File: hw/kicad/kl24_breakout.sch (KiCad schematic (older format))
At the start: 8 parts

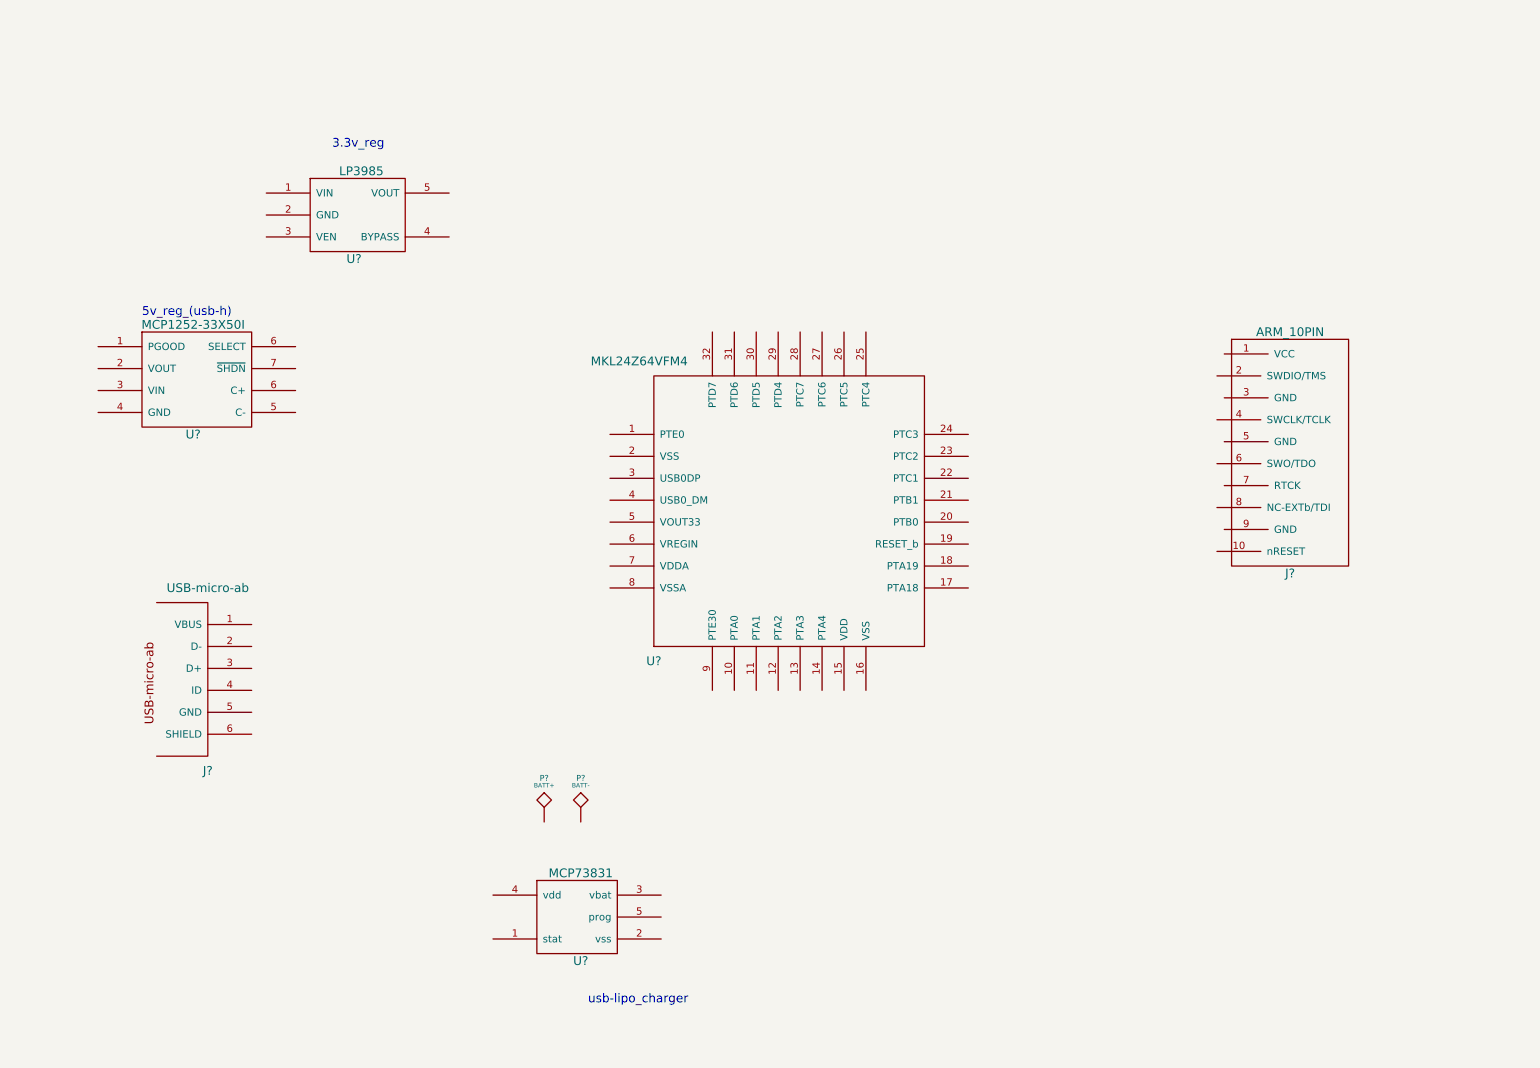
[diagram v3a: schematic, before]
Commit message: - add 0.9v lv battery powered supply (probably nopop)
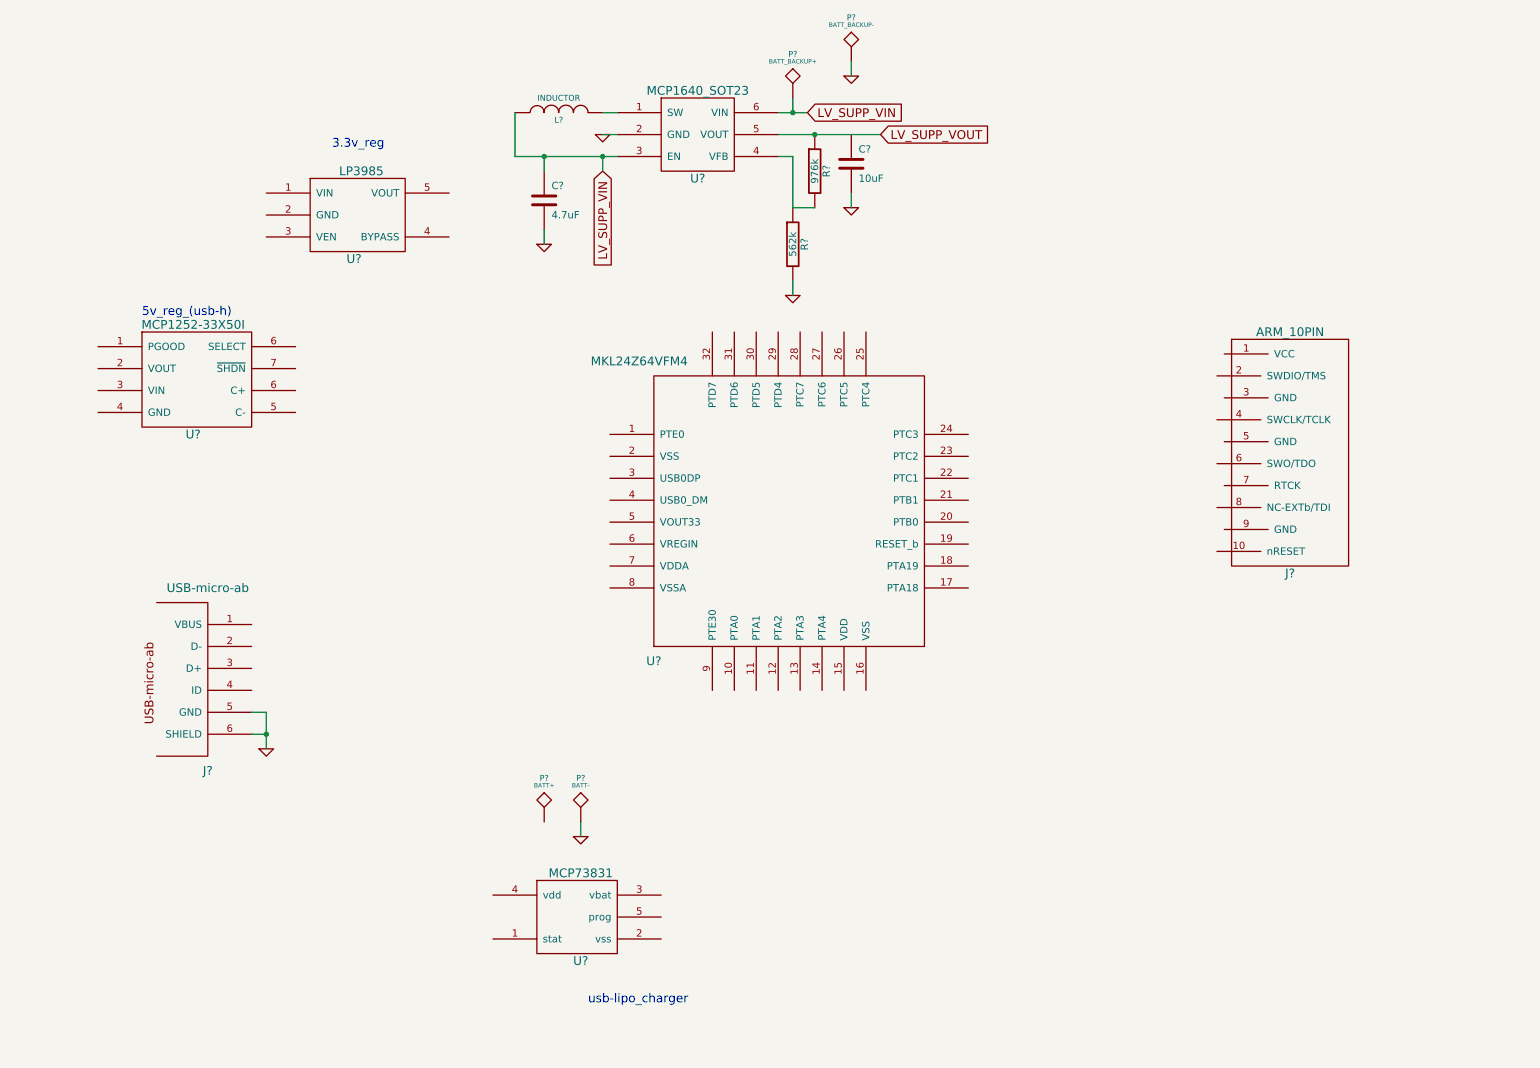
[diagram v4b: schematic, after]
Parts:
- added C?: 4.7uF, symbol C
- added C?: 10uF, symbol C
- added L?: INDUCTOR, symbol INDUCTOR
- added P?: BATT_BACKUP+, symbol TST
- added P?: BATT_BACKUP-, symbol TST
- added R?: 976k, symbol R
- added R?: 562k, symbol R
- added U?: MCP1640_SOT23, symbol MCP1640_SOT23
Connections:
- net GND: now reaches J?.5 (GND)
- net GND: now also J?.6 (SHIELD), P?.1, C?.2, C?.2, P?.1, R?.2, U?.2 (GND)
- new net: L?.2, U?.1 (SW)
- new net: R?.1, R?.2, U?.4 (VFB)
- new net LV_SUPP_VIN: C?.1, L?.1, P?.1, U?.3 (EN), U?.6 (VIN)
- new net LV_SUPP_VOUT: R?.1, U?.5 (VOUT)
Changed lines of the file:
@@
-EESchema Schematic File Version 2  date 3/5/2013 1:18:51 PM
+EESchema Schematic File Version 2  date 3/9/2013 12:18:49 PM
 LIBS:power
 LIBS:device
@@
 Sheet 1 1
 Title ""
-Date "5 mar 2013"
+Date "9 mar 2013"
 Rev ""
 Comp ""
@@
 Comment4 ""
 $EndDescr
+Connection ~ 4250 1400
+Wire Wire Line
+	4750 1400 4050 1400
+Wire Wire Line
+	4050 1400 4050 1100
+Wire Wire Line
+	4250 1400 4250 1500
+Wire Wire Line
+	6350 1650 6350 1750
+Wire Wire Line
+	5950 2250 5950 2350
+Wire Wire Line
+	6100 1750 5950 1750
+Wire Wire Line
+	4650 1250 4750 1250
+Wire Wire Line
+	4650 1400 4650 1500
+Wire Wire Line
+	5950 1100 5950 1000
+Wire Wire Line
+	2350 5350 2250 5350
+Wire Wire Line
+	6350 750  6350 850
+Wire Wire Line
+	4500 6050 4500 5950
+Wire Wire Line
+	2250 5200 2350 5200
+Wire Wire Line
+	2350 5200 2350 5450
+Connection ~ 2350 5350
+Wire Wire Line
+	6050 1100 5850 1100
+Connection ~ 5950 1100
+Connection ~ 4650 1400
+Wire Wire Line
+	5950 1750 5950 1400
+Wire Wire Line
+	5950 1400 5850 1400
+Connection ~ 6100 1250
+Wire Wire Line
+	6550 1250 5850 1250
+Wire Wire Line
+	4750 1100 4650 1100
+Wire Wire Line
+	4250 1900 4250 2000
+$Comp
+L INDUCTOR L?
+U 1 1 513B6D74
+P 4350 1100
+F 0 "L?" V 4300 1100 40  0000 C CNN
+F 1 "INDUCTOR" V 4450 1100 40  0000 C CNN
+	1    4350 1100
+	0    -1   -1   0
+$EndComp
+$Comp
+L GND #PWR?
+U 1 1 513B6CEE
+P 6350 1750
+F 0 "#PWR?" H 6350 1750 30  0001 C CNN
+F 1 "GND" H 6350 1680 30  0001 C CNN
+	1    6350 1750
+	1    0    0    -1
+$EndComp
+Text GLabel 6550 1250 2    60   Input ~ 0
+LV_SUPP_VOUT
+$Comp
+L C C?
+U 1 1 513B6C7D
+P 6350 1450
+F 0 "C?" H 6400 1550 50  0000 L CNN
+F 1 "10uF" H 6400 1350 50  0000 L CNN
+	1    6350 1450
+	1    0    0    -1
+$EndComp
+$Comp
+L GND #PWR?
+U 1 1 513B6C70
+P 5950 2350
+F 0 "#PWR?" H 5950 2350 30  0001 C CNN
+F 1 "GND" H 5950 2280 30  0001 C CNN
+	1    5950 2350
+	1    0    0    -1
+$EndComp
+$Comp
+L R R?
+U 1 1 513B6C55
+P 5950 2000
+F 0 "R?" V 6030 2000 50  0000 C CNN
+F 1 "562k" V 5950 2000 50  0000 C CNN
+	1    5950 2000
+	1    0    0    -1
+$EndComp
+$Comp
+L R R?
+U 1 1 513B6C46
+P 6100 1500
+F 0 "R?" V 6180 1500 50  0000 C CNN
+F 1 "976k" V 6100 1500 50  0000 C CNN
+	1    6100 1500
+	1    0    0    -1
+$EndComp
+$Comp
+L GND #PWR?
+U 1 1 513B6C39
+P 4650 1250
+F 0 "#PWR?" H 4650 1250 30  0001 C CNN
+F 1 "GND" H 4650 1180 30  0001 C CNN
+	1    4650 1250
+	1    0    0    -1
+$EndComp
+$Comp
+L GND #PWR?
+U 1 1 513B6C33
+P 4250 2000
+F 0 "#PWR?" H 4250 2000 30  0001 C CNN
+F 1 "GND" H 4250 1930 30  0001 C CNN
+	1    4250 2000
+	1    0    0    -1
+$EndComp
+$Comp
+L C C?
+U 1 1 513B6BF6
+P 4250 1700
+F 0 "C?" H 4300 1800 50  0000 L CNN
+F 1 "4.7uF" H 4300 1600 50  0000 L CNN
+	1    4250 1700
+	1    0    0    -1
+$EndComp
+Text GLabel 4650 1500 3    60   Input ~ 0
+LV_SUPP_VIN
+Text GLabel 6050 1100 2    60   Input ~ 0
+LV_SUPP_VIN
+$Comp
+L GND #PWR?
+U 1 1 513B6B06
+P 2350 5450
+F 0 "#PWR?" H 2350 5450 30  0001 C CNN
+F 1 "GND" H 2350 5380 30  0001 C CNN
+	1    2350 5450
+	1    0    0    -1
+$EndComp
+$Comp
+L GND #PWR?
+U 1 1 513B6AFE
+P 4500 6050
+F 0 "#PWR?" H 4500 6050 30  0001 C CNN
+F 1 "GND" H 4500 5980 30  0001 C CNN
+	1    4500 6050
+	1    0    0    -1
+$EndComp
+$Comp
+L GND #PWR?
+U 1 1 513B6A86
+P 6350 850
+F 0 "#PWR?" H 6350 850 30  0001 C CNN
+F 1 "GND" H 6350 780 30  0001 C CNN
+	1    6350 850
+	1    0    0    -1
+$EndComp
+$Comp
+L TST P?
+U 1 1 513B6A31
+P 6350 750
+F 0 "P?" H 6350 1050 40  0000 C CNN
+F 1 "BATT_BACKUP-" H 6350 1000 30  0000 C CNN
+	1    6350 750
+	1    0    0    -1
+$EndComp
+$Comp
+L TST P?
+U 1 1 513B6A2E
+P 5950 1000
+F 0 "P?" H 5950 1300 40  0000 C CNN
+F 1 "BATT_BACKUP+" H 5950 1250 30  0000 C CNN
+	1    5950 1000
+	1    0    0    -1
+$EndComp
+$Comp
+L MCP1640_SOT23 U?
+U 1 1 513B6A06
+P 5300 1250
+F 0 "U?" H 5300 950 60  0000 C CNN
+F 1 "MCP1640_SOT23" H 5300 1550 60  0000 C CNN
+	1    5300 1250
+	1    0    0    -1
+$EndComp
 $Comp
 L MCP73831 U?

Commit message: - add lipo charger circuit
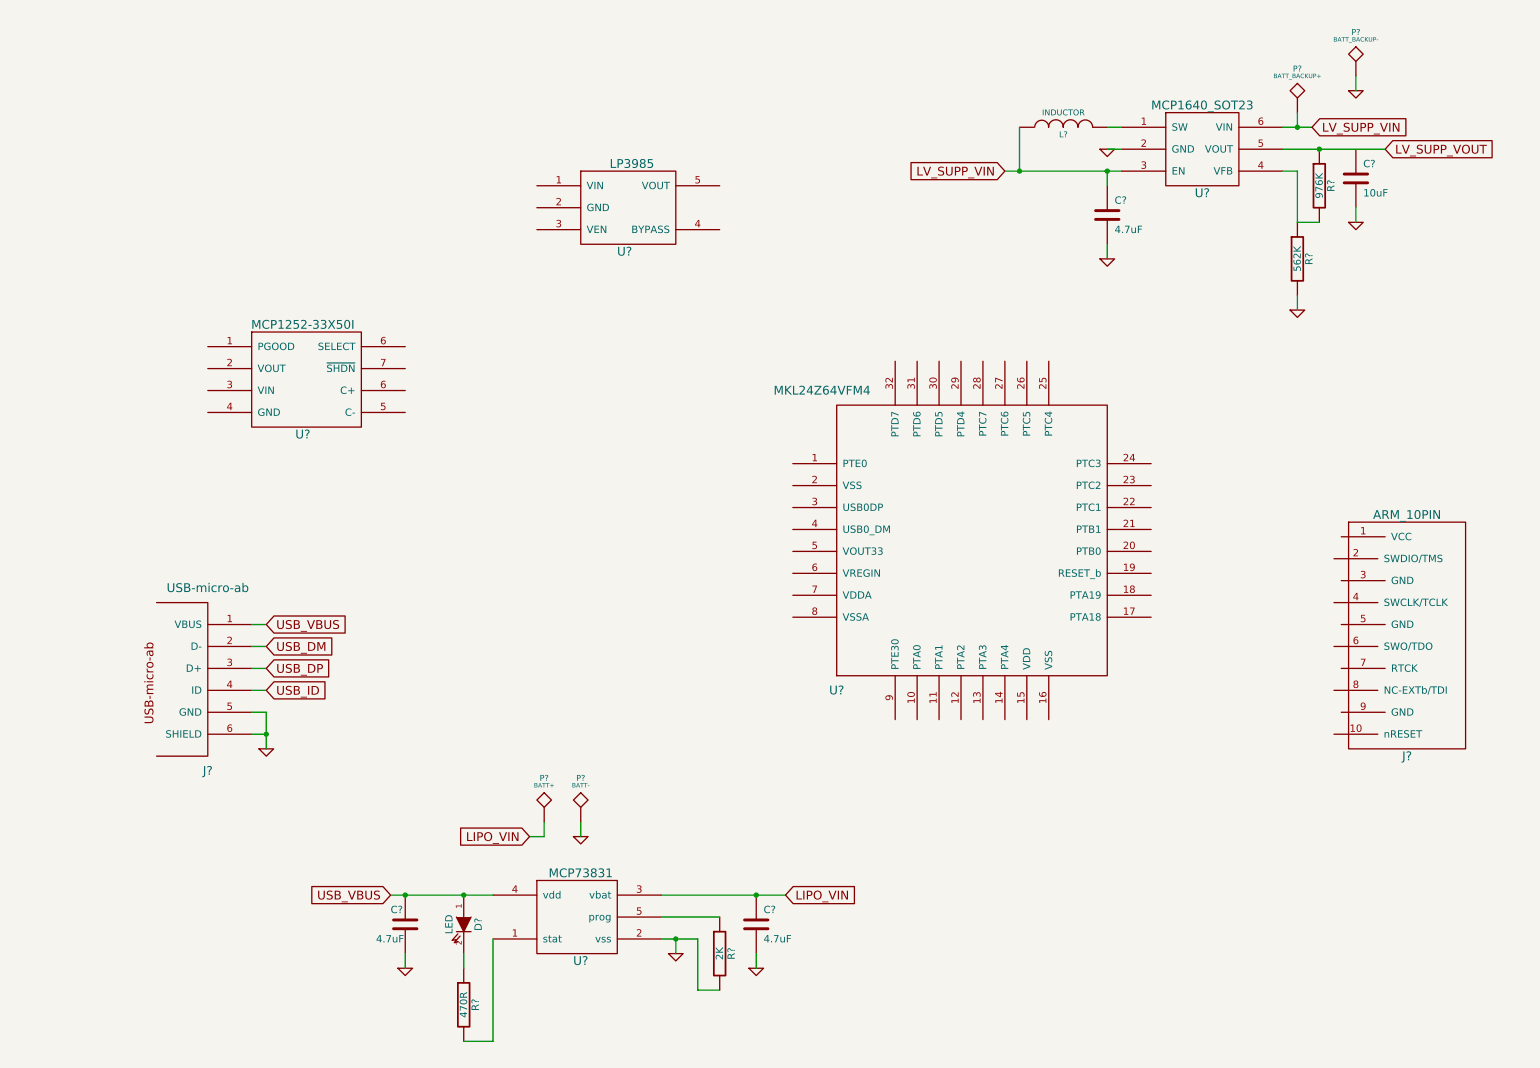
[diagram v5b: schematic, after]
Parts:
- added C? (x2): 4.7uF, symbol C
- added D?: LED, symbol LED
- added R?: 470R, symbol R
- added R?: 2K, symbol R
- R?: value 976k -> 976K
- R?: value 562k -> 562K
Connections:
- net GND: now also U?.2 (vss), C?.2, C?.2, R?.2
- net USB_VBUS: now reaches J?.1 (VBUS)
- net USB_VBUS: now also U?.4 (vdd), C?.1, D?.1 (A)
- net USB_DM: now reaches J?.2 (D-)
- net USB_DP: now reaches J?.3 (D+)
- net USB_ID: now reaches J?.4 (ID)
- net LIPO_VIN: now reaches P?.1
- net LIPO_VIN: now also U?.3 (vbat), C?.1
- net at U?.1 (stat): now also R?.2
- net at U?.5 (prog): now also R?.1
- new net: D?.2 (K), R?.1
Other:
- note removed: "3.3v_reg"
- note removed: "5v_reg_(usb-h)"
- note removed: "usb-lipo_charger"
- moved on the sheet: C?, J?, L?, P?, R?, U?
